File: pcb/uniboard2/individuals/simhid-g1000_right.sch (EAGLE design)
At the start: 73 parts, among them J4 PCB-INTERCONNECT, J5 ZX62-B-5PA(33)-FULL, J6 2212S, SW27 SLLB510100-HS, SW28 TS-1109S-B-B, SW29 TS-1109S-B-B, SW30 TS-1109S-B-B, SW31 TS-1109S-B-B, SW32 TS-1109S-B-B, SW33 TS-1109S-B-B, SW34 TS-1109S-B-B, U4 STM32F411CCU, U5 MCP23S18-E/MJ, U6 MCP1703AT-3302E/CB, X1 16MHz/10pF

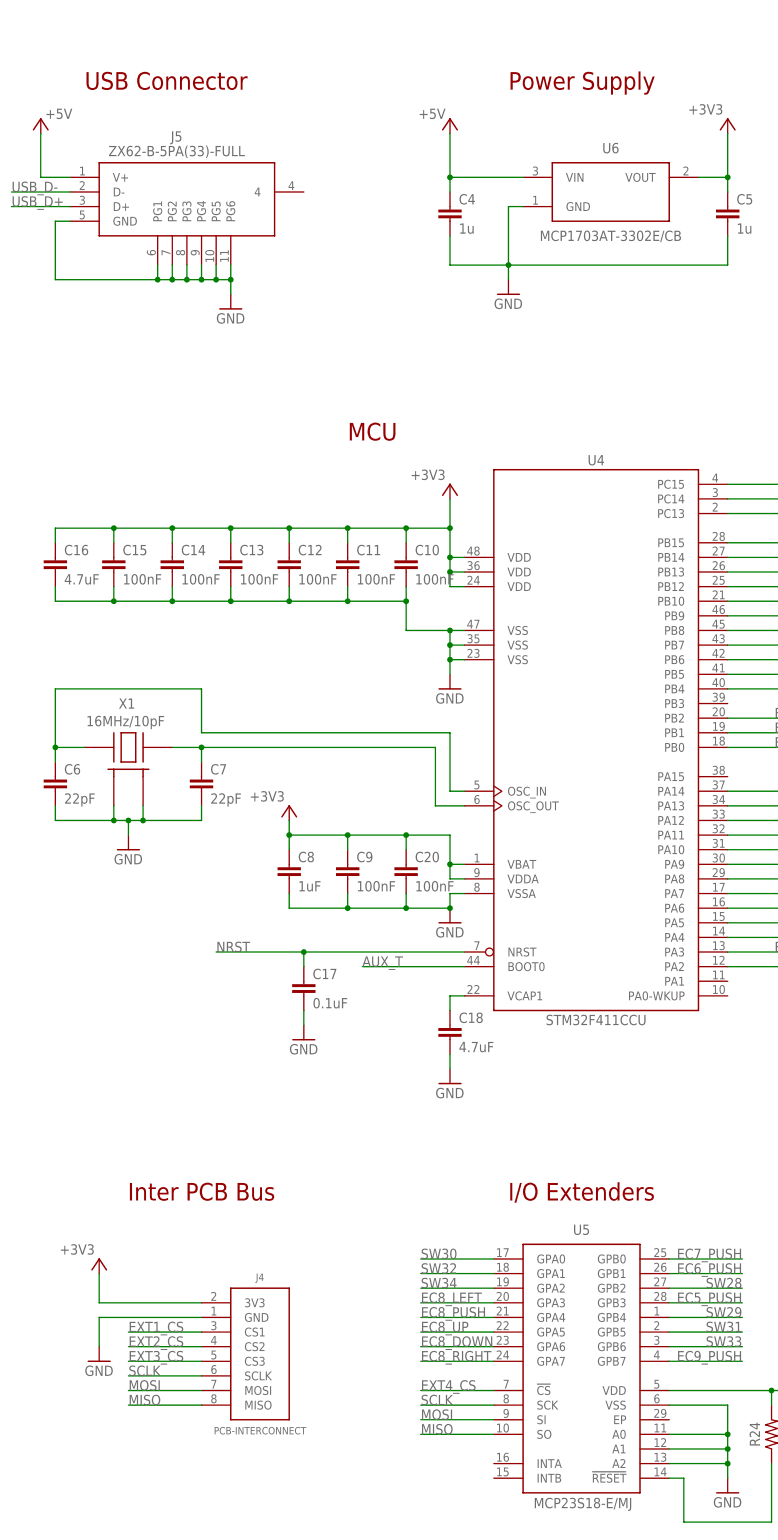
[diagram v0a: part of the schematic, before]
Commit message: Added vertical USB connector versions
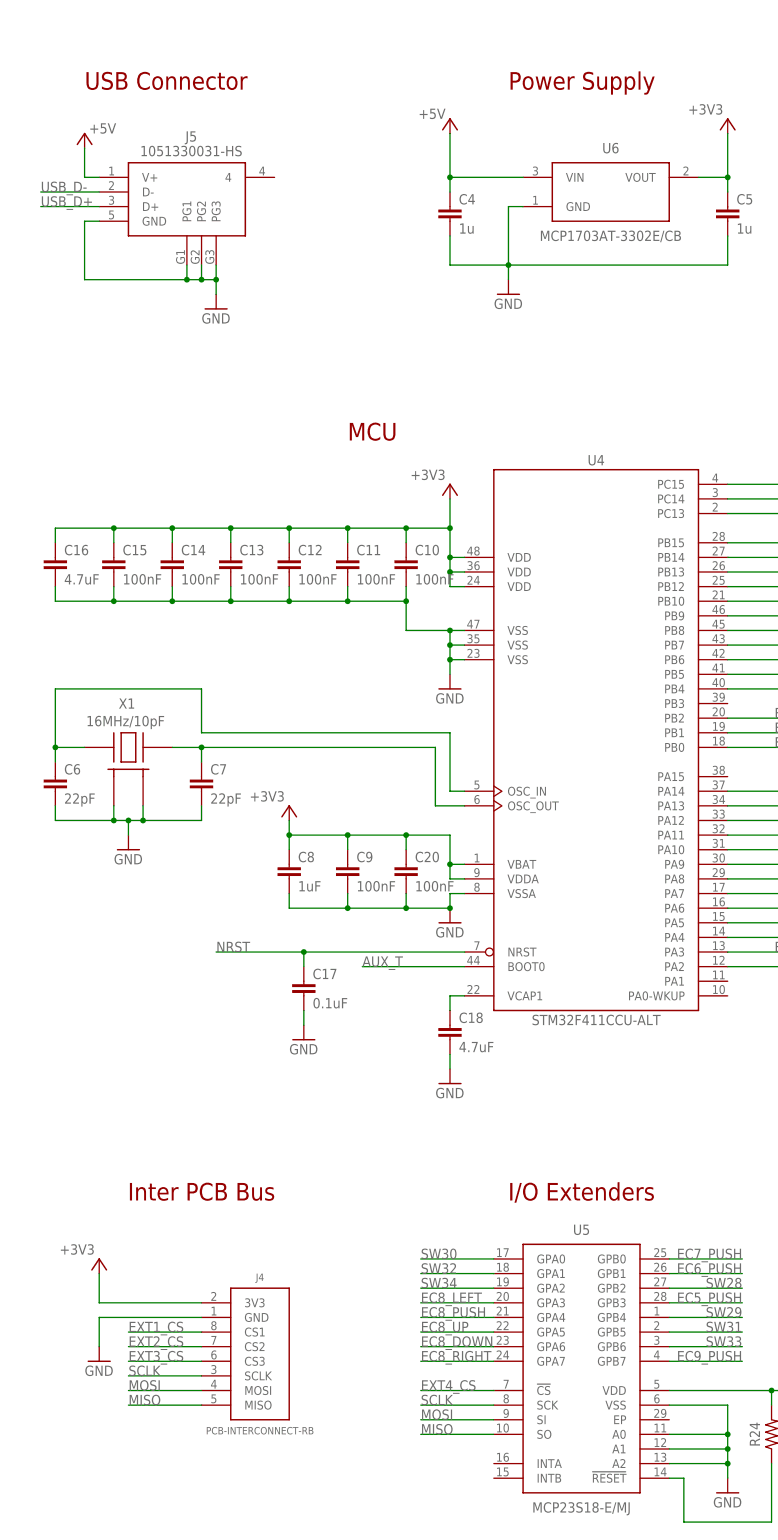
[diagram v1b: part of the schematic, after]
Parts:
- J4: value PCB-INTERCONNECT -> PCB-INTERCONNECT-RB; device SimHID-G1000:PCB-INTERCONNECT -> SimHID-G1000:PCB-INTERCONNECT-RB
- J5: value ZX62-B-5PA(33)-FULL -> 1051330031-HS; device ZX62-B-5PA(33):ZX62-B-5PA(33)-FULL -> USB-connectors:1051330031-HS
- U4: value STM32F411CCU -> STM32F411CCU-ALT; device stm32:STM32F411CCU -> stm32:STM32F411CCU-ALT
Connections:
- net GND: no longer J5.PG4, J5.PG5, J5.PG6
